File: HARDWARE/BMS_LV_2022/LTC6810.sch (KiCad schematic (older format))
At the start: 33 parts, among them J10 Conn_01x01_Female, J11 Conn_01x07_Female, J4 Conn_01x01_Female, J5 Conn_01x01_Female, J6 Conn_01x01_Female, J7 Conn_01x01_Female, J8 Conn_01x01_Female, J9 Conn_01x01_Female, Q1 BC846

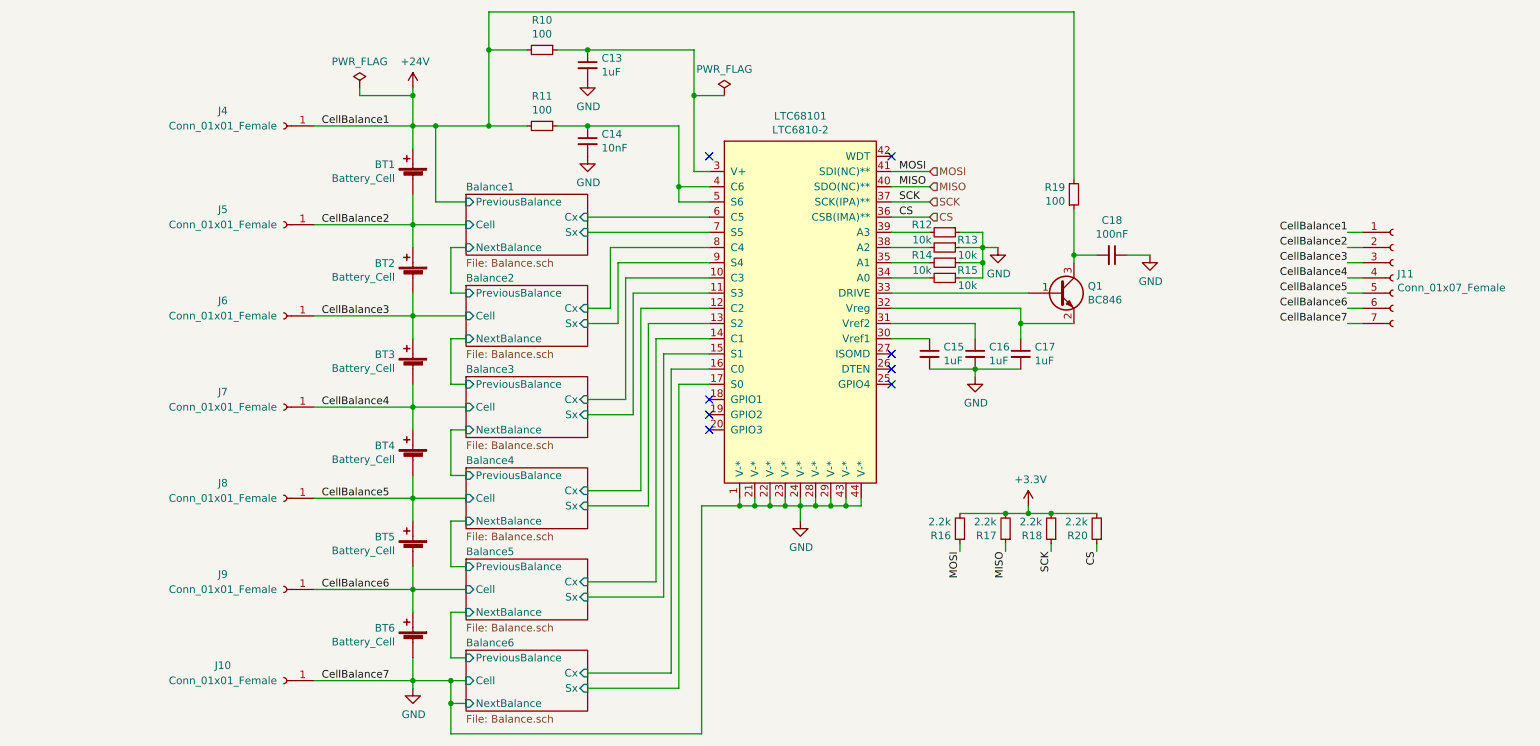
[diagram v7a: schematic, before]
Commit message: PCB Layout Update
Some work on PCB Layout
+ AS214-97PN (connector) 3D model added
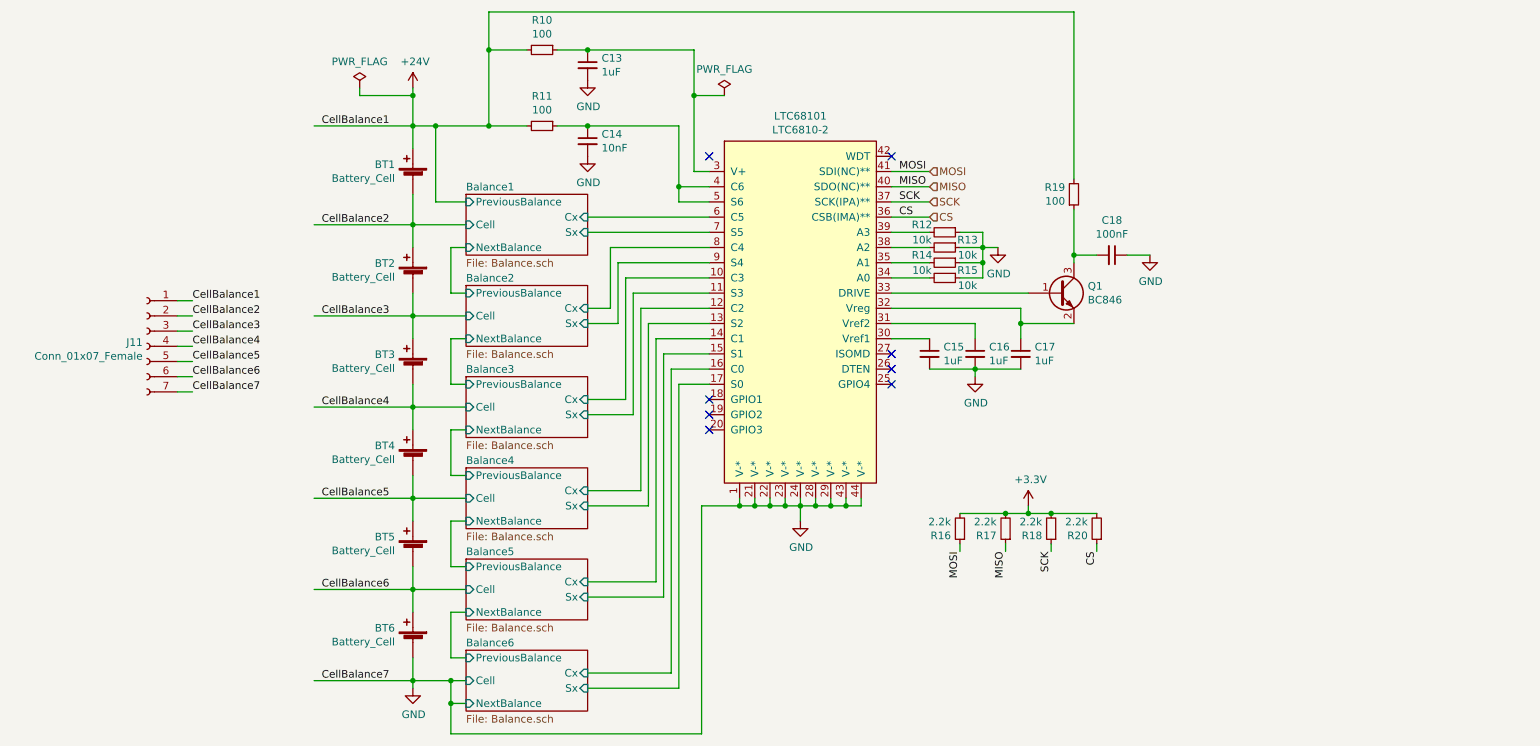
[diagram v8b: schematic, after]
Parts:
- removed J10, J4, J5, J6, J7, J8, J9: Conn_01x01_Female, Connector_PinHeader_2.54mm:PinHeader_1x01_P2.54mm_Vertical, symbol Connector:Conn_01x01_Female
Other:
- moved on the sheet: J11
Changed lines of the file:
@@
-$EndComp
-$Comp
-L Connector:Conn_01x01_Female J4
-U 1 1 61A1B6B1
-P 2650 2300
-F 0 "J4" H 3050 2400 50  0000 C CNN
-F 1 "Conn_01x01_Female" H 3050 2300 50  0000 C CNN
-F 2 "Connector_PinHeader_2.54mm:PinHeader_1x01_P2.54mm_Vertical" H 2650 2300 50  0001 C CNN
-F 3 "~" H 2650 2300 50  0001 C CNN
-	1    2650 2300
-	-1   0    0    -1
-$EndComp
-$Comp
-L Connector:Conn_01x01_Female J5
-U 1 1 61A336C9
-P 2650 2950
-F 0 "J5" H 3050 3050 50  0000 C CNN
-F 1 "Conn_01x01_Female" H 3050 2950 50  0000 C CNN
-F 2 "Connector_PinHeader_2.54mm:PinHeader_1x01_P2.54mm_Vertical" H 2650 2950 50  0001 C CNN
-F 3 "~" H 2650 2950 50  0001 C CNN
-	1    2650 2950
-	-1   0    0    -1
-$EndComp
-$Comp
-L Connector:Conn_01x01_Female J6
-U 1 1 61A9D24A
-P 2650 3550
-F 0 "J6" H 3050 3650 50  0000 C CNN
-F 1 "Conn_01x01_Female" H 3050 3550 50  0000 C CNN
-F 2 "Connector_PinHeader_2.54mm:PinHeader_1x01_P2.54mm_Vertical" H 2650 3550 50  0001 C CNN
-F 3 "~" H 2650 3550 50  0001 C CNN
-	1    2650 3550
-	-1   0    0    -1
-$EndComp
-$Comp
-L Connector:Conn_01x01_Female J7
-U 1 1 61AA88B9
-P 2650 4150
-F 0 "J7" H 3050 4250 50  0000 C CNN
-F 1 "Conn_01x01_Female" H 3050 4150 50  0000 C CNN
-F 2 "Connector_PinHeader_2.54mm:PinHeader_1x01_P2.54mm_Vertical" H 2650 4150 50  0001 C CNN
-F 3 "~" H 2650 4150 50  0001 C CNN
-	1    2650 4150
-	-1   0    0    -1
-$EndComp
-$Comp
-L Connector:Conn_01x01_Female J8
-U 1 1 61AAC32A
-P 2650 4750
-F 0 "J8" H 3050 4850 50  0000 C CNN
-F 1 "Conn_01x01_Female" H 3050 4750 50  0000 C CNN
-F 2 "Connector_PinHeader_2.54mm:PinHeader_1x01_P2.54mm_Vertical" H 2650 4750 50  0001 C CNN
-F 3 "~" H 2650 4750 50  0001 C CNN
-	1    2650 4750
-	-1   0    0    -1
-$EndComp
-$Comp
-L Connector:Conn_01x01_Female J9
-U 1 1 61AAFFF2
-P 2650 5350
-F 0 "J9" H 3050 5450 50  0000 C CNN
-F 1 "Conn_01x01_Female" H 3050 5350 50  0000 C CNN
-F 2 "Connector_PinHeader_2.54mm:PinHeader_1x01_P2.54mm_Vertical" H 2650 5350 50  0001 C CNN
-F 3 "~" H 2650 5350 50  0001 C CNN
-	1    2650 5350
-	-1   0    0    -1
-$EndComp
-$Comp
-L Connector:Conn_01x01_Female J10
-U 1 1 61AB3B1A
-P 2650 5950
-F 0 "J10" H 3050 6050 50  0000 C CNN
-F 1 "Conn_01x01_Female" H 3050 5950 50  0000 C CNN
-F 2 "Connector_PinHeader_2.54mm:PinHeader_1x01_P2.54mm_Vertical" H 2650 5950 50  0001 C CNN
-F 3 "~" H 2650 5950 50  0001 C CNN
-	1    2650 5950
-	-1   0    0    -1
 $EndComp
 $Comp
@@
 Text Label 2900 5950 0    50   ~ 0
 CellBalance7
-Text Label 9650 3000 2    50   ~ 0
+Text Label 2050 3450 0    50   ~ 0
 CellBalance1
-Text Label 9650 3100 2    50   ~ 0
+Text Label 2050 3550 0    50   ~ 0
 CellBalance2
-Text Label 9650 3200 2    50   ~ 0
+Text Label 2050 3650 0    50   ~ 0
 CellBalance3
-Text Label 9650 3300 2    50   ~ 0
+Text Label 2050 3750 0    50   ~ 0
 CellBalance4
-Text Label 9650 3400 2    50   ~ 0
+Text Label 2050 3850 0    50   ~ 0
 CellBalance5
-Text Label 9650 3500 2    50   ~ 0
+Text Label 2050 3950 0    50   ~ 0
 CellBalance6
-Text Label 9650 3600 2    50   ~ 0
+Text Label 2050 4050 0    50   ~ 0
 CellBalance7
 $Comp
 L Connector:Conn_01x07_Female J11
 U 1 1 61DCAD61
-P 9950 3300
-F 0 "J11" H 9978 3326 50  0000 L CNN
-F 1 "Conn_01x07_Female" H 9978 3235 50  0000 L CNN
-F 2 "Connector_JST:JST_XH_B7B-XH-A_1x07_P2.50mm_Vertical" H 9950 3300 50  0001 C CNN
-F 3 "~" H 9950 3300 50  0001 C CNN
-	1    9950 3300
-	1    0    0    -1
+P 1750 3750
+F 0 "J11" H 1778 3776 50  0000 L CNN
+F 1 "Conn_01x07_Female" H 1778 3685 50  0000 L CNN
+F 2 "Connector_JST:JST_XH_B7B-XH-A_1x07_P2.50mm_Vertical" H 1750 3750 50  0001 C CNN
+F 3 "~" H 1750 3750 50  0001 C CNN
+	1    1750 3750
+	-1   0    0    -1
 $EndComp
 Wire Wire Line
-	9650 3000 9750 3000
+	2050 3450 1950 3450
 Wire Wire Line
-	9650 3100 9750 3100
+	2050 3550 1950 3550
 Wire Wire Line
-	9650 3200 9750 3200
+	2050 3650 1950 3650
 Wire Wire Line
-	9650 3300 9750 3300
+	2050 3750 1950 3750
 Wire Wire Line
-	9650 3400 9750 3400
+	2050 3850 1950 3850
 Wire Wire Line
-	9650 3500 9750 3500
+	2050 3950 1950 3950
 Wire Wire Line
-	9650 3600 9750 3600
+	2050 4050 1950 4050
 $EndSCHEMATC
